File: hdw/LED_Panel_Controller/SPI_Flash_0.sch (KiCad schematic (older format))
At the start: 14 parts, among them U2401 74LVC1G97, U2402 SST25VF080B-50-4I-S2AF

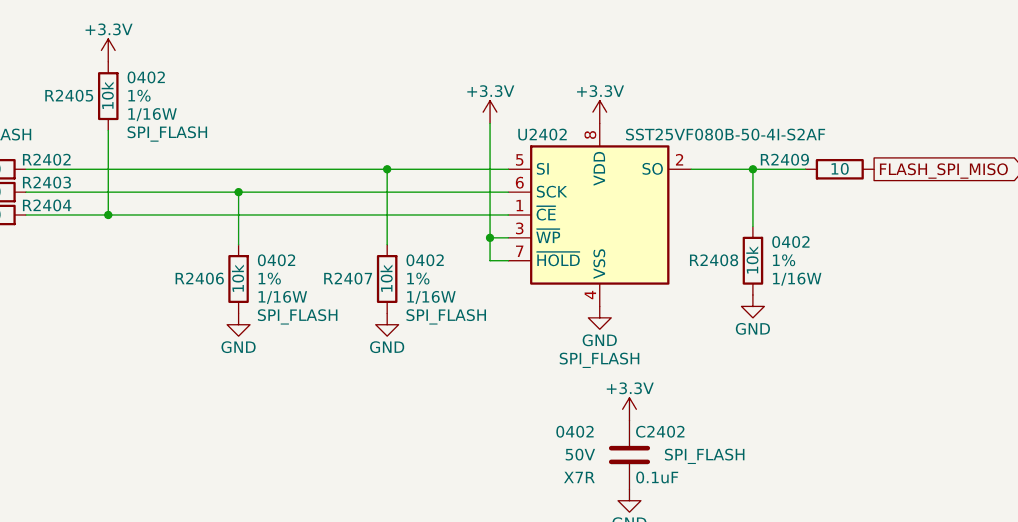
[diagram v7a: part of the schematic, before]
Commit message: fixed SPI flash pull resistors, more PCB placement
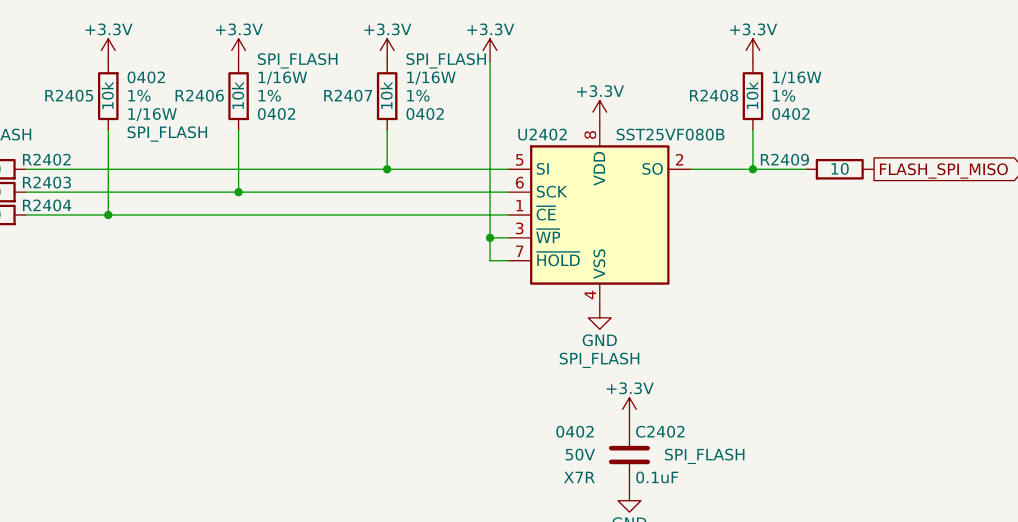
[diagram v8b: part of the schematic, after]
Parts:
- U2402: value SST25VF080B-50-4I-S2AF -> SST25VF080B
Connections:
- net +3V3: now also R2406.2, R2407.2, R2408.2
- net GND: no longer R2406.2, R2407.2, R2408.2
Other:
- moved on the sheet: R2406, R2407, R2408
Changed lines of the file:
@@
 L Custom_Library:R_Custom R2408
 U 1 1 60786269
-P 6750 3850
-F 0 "R2408" H 6690 3850 50  0000 R CNN
-F 1 "10k" V 6750 3850 50  0000 C CNN
-F 2 "Resistors_SMD:R_0402" H 6750 3850 50  0001 C CNN
-F 3 "" H 6750 3850 50  0001 C CNN
-F 4 "0402" H 6830 3930 50  0000 L CNN "display_footprint"
-F 5 "1%" H 6830 3850 50  0000 L CNN "Tolerance"
-F 6 "1/16W" H 6830 3770 50  0000 L CNN "Wattage"
-F 7 "RMCF0402FT10K0CT-ND" H 7050 4250 60  0001 C CNN "Digi-Key PN"
-	1    6750 3850
-	1    0    0    -1
-$EndComp
-$Comp
-L power:GND #PWR02408
-U 1 1 6078626F
-P 5150 4080
-F 0 "#PWR02408" H 5150 3830 50  0001 C CNN
-F 1 "GND" H 5150 3930 50  0000 C CNN
-F 2 "" H 5150 4080 50  0001 C CNN
-F 3 "" H 5150 4080 50  0001 C CNN
-	1    5150 4080
-	1    0    0    -1
-$EndComp
-$Comp
-L power:GND #PWR02414
-U 1 1 60786278
-P 6750 4000
-F 0 "#PWR02414" H 6750 3750 50  0001 C CNN
-F 1 "GND" H 6750 3850 50  0000 C CNN
-F 2 "" H 6750 4000 50  0001 C CNN
-F 3 "" H 6750 4000 50  0001 C CNN
-	1    6750 4000
-	1    0    0    -1
+P 6750 3130
+F 0 "R2408" H 6690 3130 50  0000 R CNN
+F 1 "10k" V 6750 3130 50  0000 C CNN
+F 2 "Resistors_SMD:R_0402" H 6750 3130 50  0001 C CNN
+F 3 "" H 6750 3130 50  0001 C CNN
+F 4 "0402" H 6830 3210 50  0000 L CNN "display_footprint"
+F 5 "1%" H 6830 3130 50  0000 L CNN "Tolerance"
+F 6 "1/16W" H 6830 3050 50  0000 L CNN "Wattage"
+F 7 "RMCF0402FT10K0CT-ND" H 7050 3530 60  0001 C CNN "Digi-Key PN"
+	1    6750 3130
+	1    0    0    1
 $EndComp
 $Comp
@@
 $EndComp
 Wire Wire Line
-	5150 3450 5150 3780
-Connection ~ 5150 3450
-Wire Wire Line
-	5150 3450 5680 3450
-Wire Wire Line
 	3930 3280 3930 3650
 Wire Wire Line
 	3930 3650 5680 3650
 Connection ~ 3930 3650
-Wire Wire Line
-	6980 3450 6750 3450
-Wire Wire Line
-	6750 3700 6750 3450
-Connection ~ 6750 3450
-Wire Wire Line
-	6750 3450 6480 3450
 Text GLabel 7280 3450 2    50   Output ~ 0
 FLASH_SPI_MISO
@@
 $EndComp
 $Comp
-L Memory_Flash:SST25VF080B-50-4x-S2Ax U2402
-U 1 1 607862FC
-P 6080 3650
-F 0 "U2402" H 5830 4000 50  0000 C CNN
-F 1 "SST25VF080B-50-4I-S2AF" H 6630 4000 50  0000 C CNN
-F 2 "Package_SO:SOIC-8_5.275x5.275mm_P1.27mm" H 6080 2950 50  0001 C CNN
-F 3 "http://ww1.microchip.com/downloads/en/DeviceDoc/20005045C.pdf" H 6030 4200 50  0001 C CNN
-F 4 "SST25VF080B-50-4I-S2AE-T" H 6080 3650 50  0001 C CNN "Digi-Key PN"
-F 5 "SPI_FLASH" H 6080 3020 50  0000 C CNN "Configuration"
-	1    6080 3650
-	1    0    0    -1
-$EndComp
-$Comp
 L power:+3.3V #PWR02412
 U 1 1 5F689292
@@
 L power:+3.3V #PWR02409
 U 1 1 60786311
-P 5600 3250
-F 0 "#PWR02409" H 5600 3100 50  0001 C CNN
-F 1 "+3.3V" H 5600 3390 50  0000 C CNN
-F 2 "" H 5600 3250 50  0001 C CNN
-F 3 "" H 5600 3250 50  0001 C CNN
-	1    5600 3250
+P 5600 2980
+F 0 "#PWR02409" H 5600 2830 50  0001 C CNN
+F 1 "+3.3V" H 5600 3120 50  0000 C CNN
+F 2 "" H 5600 2980 50  0001 C CNN
+F 3 "" H 5600 2980 50  0001 C CNN
+	1    5600 2980
 	1    0    0    -1
 $EndComp
@@
 	5680 3750 5600 3750
 Wire Wire Line
-	5600 3750 5600 3250
+	5600 3750 5600 2980
 Wire Wire Line
 	5680 3850 5600 3850
@@
 	5600 3850 5600 3750
 Connection ~ 5600 3750
-Wire Wire Line
-	3570 3550 4500 3550
 $Comp
 L Custom_Library:R_Custom R2406
 U 1 1 60786314
-P 4500 3930
-F 0 "R2406" H 4440 3930 50  0000 R CNN
-F 1 "10k" V 4500 3930 50  0000 C CNN
-F 2 "Resistors_SMD:R_0402" H 4500 3930 50  0001 C CNN
-F 3 "" H 4500 3930 50  0001 C CNN
-F 4 "0402" H 4580 4010 50  0000 L CNN "display_footprint"
-F 5 "1%" H 4580 3930 50  0000 L CNN "Tolerance"
-F 6 "1/16W" H 4580 3850 50  0000 L CNN "Wattage"
-F 7 "RMCF0402FT10K0CT-ND" H 4800 4330 60  0001 C CNN "Digi-Key PN"
-F 8 "SPI_FLASH" H 4580 3770 50  0000 L CNN "Configuration"
-	1    4500 3930
-	1    0    0    -1
-$EndComp
-$Comp
-L power:GND #PWR02407
-U 1 1 60786319
-P 4500 4080
-F 0 "#PWR02407" H 4500 3830 50  0001 C CNN
-F 1 "GND" H 4500 3930 50  0000 C CNN
-F 2 "" H 4500 4080 50  0001 C CNN
-F 3 "" H 4500 4080 50  0001 C CNN
-	1    4500 4080
-	1    0    0    -1
-$EndComp
-Wire Wire Line
-	3570 3450 5150 3450
-Wire Wire Line
-	4500 3550 4500 3780
-Connection ~ 4500 3550
-Wire Wire Line
-	4500 3550 5680 3550
+P 4500 3130
+F 0 "R2406" H 4440 3130 50  0000 R CNN
+F 1 "10k" V 4500 3130 50  0000 C CNN
+F 2 "Resistors_SMD:R_0402" H 4500 3130 50  0001 C CNN
+F 3 "" H 4500 3130 50  0001 C CNN
+F 4 "0402" H 4580 3210 50  0000 L CNN "display_footprint"
+F 5 "1%" H 4580 3130 50  0000 L CNN "Tolerance"
+F 6 "1/16W" H 4580 3050 50  0000 L CNN "Wattage"
+F 7 "RMCF0402FT10K0CT-ND" H 4800 3530 60  0001 C CNN "Digi-Key PN"
+F 8 "SPI_FLASH" H 4580 2970 50  0000 L CNN "Configuration"
+	1    4500 3130
+	1    0    0    1
+$EndComp
 $Comp
 L Custom_Library:R_Custom R2403
@@
 L Custom_Library:R_Custom R2407
 U 1 1 60786355
-P 5150 3930
-F 0 "R2407" H 5090 3930 50  0000 R CNN
-F 1 "10k" V 5150 3930 50  0000 C CNN
-F 2 "Resistors_SMD:R_0402" H 5150 3930 50  0001 C CNN
-F 3 "" H 5150 3930 50  0001 C CNN
-F 4 "0402" H 5230 4010 50  0000 L CNN "display_footprint"
-F 5 "1%" H 5230 3930 50  0000 L CNN "Tolerance"
-F 6 "1/16W" H 5230 3850 50  0000 L CNN "Wattage"
-F 7 "RMCF0402FT10K0CT-ND" H 5450 4330 60  0001 C CNN "Digi-Key PN"
-F 8 "SPI_FLASH" H 5230 3770 50  0000 L CNN "Configuration"
-	1    5150 3930
-	1    0    0    -1
+P 5150 3130
+F 0 "R2407" H 5090 3130 50  0000 R CNN
+F 1 "10k" V 5150 3130 50  0000 C CNN
+F 2 "Resistors_SMD:R_0402" H 5150 3130 50  0001 C CNN
+F 3 "" H 5150 3130 50  0001 C CNN
+F 4 "0402" H 5230 3210 50  0000 L CNN "display_footprint"
+F 5 "1%" H 5230 3130 50  0000 L CNN "Tolerance"
+F 6 "1/16W" H 5230 3050 50  0000 L CNN "Wattage"
+F 7 "RMCF0402FT10K0CT-ND" H 5450 3530 60  0001 C CNN "Digi-Key PN"
+F 8 "SPI_FLASH" H 5230 2970 50  0000 L CNN "Configuration"
+	1    5150 3130
+	1    0    0    1
 $EndComp
 $Comp
@@
 	1    0    0    -1
 $EndComp
+Wire Wire Line
+	3570 3450 5150 3450
+Wire Wire Line
+	3570 3550 4500 3550
+Wire Wire Line
+	6480 3450 6750 3450
+Wire Wire Line
+	6750 3280 6750 3450
+Connection ~ 6750 3450
+Wire Wire Line
+	6750 3450 6980 3450
+$Comp
+L Memory_Flash:SST25VF080B-50-4x-S2Ax U2402
+U 1 1 607862FC
+P 6080 3650
+F 0 "U2402" H 5830 4000 50  0000 C CNN
+F 1 "SST25VF080B" H 6630 4000 50  0000 R CNN
+F 2 "Package_SO:SOIC-8_5.275x5.275mm_P1.27mm" H 6080 2950 50  0001 C CNN
+F 3 "http://ww1.microchip.com/downloads/en/DeviceDoc/20005045C.pdf" H 6030 4200 50  0001 C CNN
+F 4 "SST25VF080B-50-4I-S2AE-T" H 6080 3650 50  0001 C CNN "Digi-Key PN"
+F 5 "SPI_FLASH" H 6080 3020 50  0000 C CNN "Configuration"
+	1    6080 3650
+	1    0    0    -1
+$EndComp
+$Comp
+L power:+3.3V #PWR0103
+U 1 1 60670095
+P 6750 2980
+F 0 "#PWR0103" H 6750 2830 50  0001 C CNN
+F 1 "+3.3V" H 6750 3120 50  0000 C CNN
+F 2 "" H 6750 2980 50  0001 C CNN
+F 3 "" H 6750 2980 50  0001 C CNN
+	1    6750 2980
+	1    0    0    -1
+$EndComp
+$Comp
+L power:+3.3V #PWR0104
+U 1 1 6067048F
+P 5150 2980
+F 0 "#PWR0104" H 5150 2830 50  0001 C CNN
+F 1 "+3.3V" H 5150 3120 50  0000 C CNN
+F 2 "" H 5150 2980 50  0001 C CNN
+F 3 "" H 5150 2980 50  0001 C CNN
+	1    5150 2980
+	1    0    0    -1
+$EndComp
+$Comp
+L power:+3.3V #PWR0105
+U 1 1 6067080C
+P 4500 2980
+F 0 "#PWR0105" H 4500 2830 50  0001 C CNN
+F 1 "+3.3V" H 4500 3120 50  0000 C CNN
+F 2 "" H 4500 2980 50  0001 C CNN
+F 3 "" H 4500 2980 50  0001 C CNN
+	1    4500 2980
+	1    0    0    -1
+$EndComp
+Wire Wire Line
+	4500 3280 4500 3550
+Connection ~ 4500 3550
+Wire Wire Line
+	4500 3550 5680 3550
+Wire Wire Line
+	5150 3280 5150 3450
+Connection ~ 5150 3450
+Wire Wire Line
+	5150 3450 5680 3450
 $EndSCHEMATC
